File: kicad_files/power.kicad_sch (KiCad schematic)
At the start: 22 parts, among them J10 Battery Connector, U11 LT1963AxST-3.3, U14 TPS54331DR

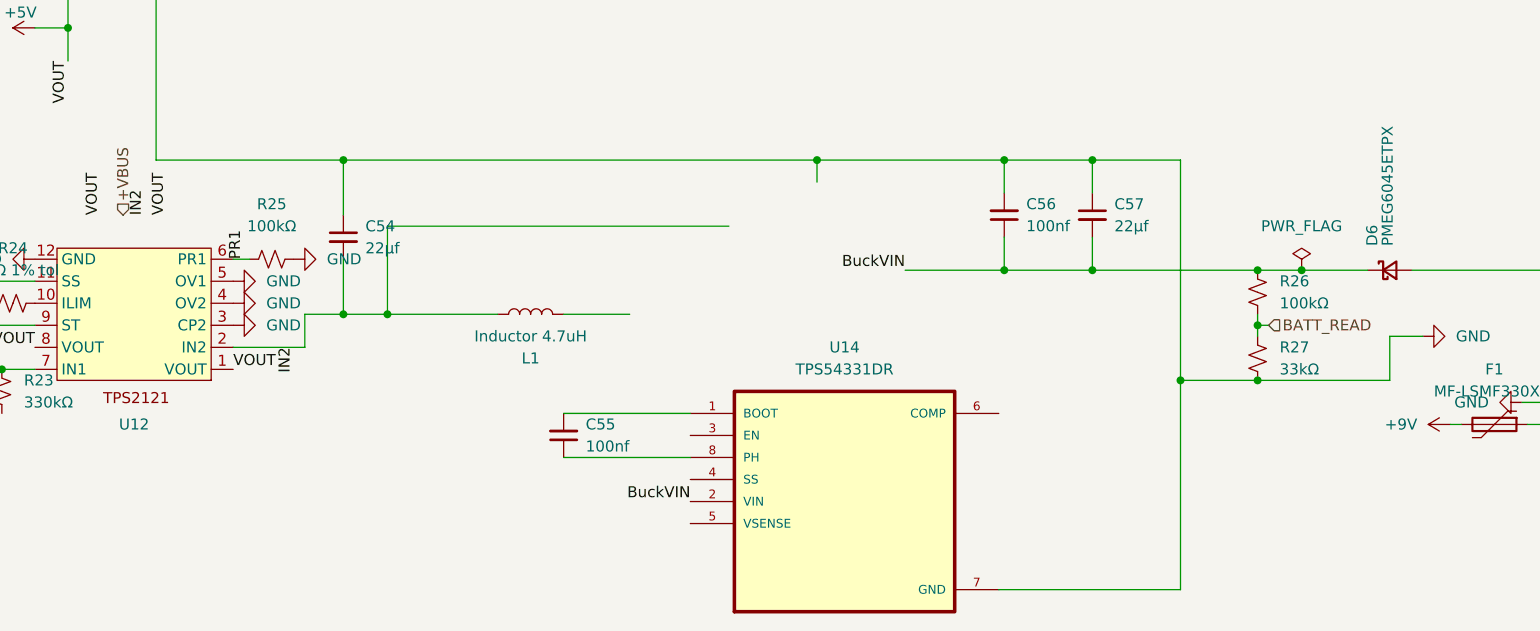
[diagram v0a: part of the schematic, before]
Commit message: fix schem for buck conv
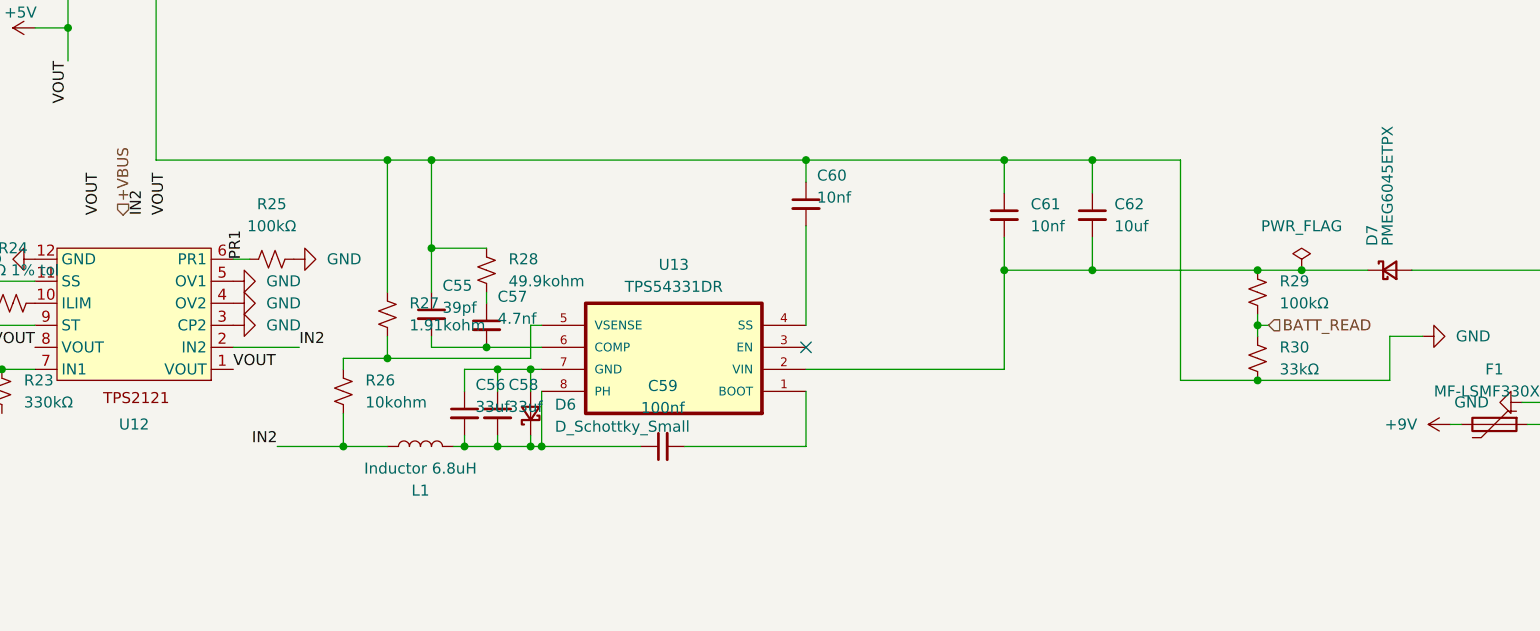
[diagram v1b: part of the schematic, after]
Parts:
- removed C54: 22μf, Capacitor_SMD:C_0805_2012Metric, symbol Device:C_Small
- added C55: 39pf, Capacitor_SMD:C_0402_1005Metric, symbol Device:C_Small
- added C58: 33uf, Capacitor_SMD:C_0805_2012Metric, symbol Device:C_Small
- added C60, C61: 10nf, Capacitor_SMD:C_0402_1005Metric, symbol Device:C_Small
- added C62: 10uf, Capacitor_SMD:C_0805_2012Metric, symbol Device:C_Small
- added D6: D_Schottky_Small, Diode_SMD:D_SMA, symbol Device:D_Schottky_Small
- added R26: 10kohm, Resistor_SMD:R_0402_1005Metric, symbol Device:R_Small_US
- added R27: 1.91kohm, Resistor_SMD:R_0402_1005Metric, symbol Device:R_Small_US
- added R28: 49.9kohm, Resistor_SMD:R_0402_1005Metric, symbol Device:R_Small_US
- C56: value 100nf -> 33uf; footprint Capacitor_SMD:C_0402_1005Metric -> Capacitor_SMD:C_0805_2012Metric
- C57: value 22μf -> 4.7nf; footprint Capacitor_SMD:C_0805_2012Metric -> Capacitor_SMD:C_0402_1005Metric
- L1: value Inductor 4.7uH -> Inductor 6.8uH
- renumbered C55 to C59, D6 to D7, R26 to R29, R27 to R30, U14 to U13
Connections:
- net GND: now also C55.1, C60.1, C61.1, C62.1, R27.1, R28.1; no longer C56.2, C57.1, U13.7 (GND)
- net IN2: now also R26.2
- net at C59.1, U13.8 (PH): now also C56.2, L1.2, C58.2, D6.1 (K)
- net at U13.4 (SS): now also C60.2
- net at U13.5 (VSENSE): now also R26.1, R27.2
- net at U13.6 (COMP): now also C57.2, C55.2
- net BuckVIN: no longer names the net of D7.1 (K), R29.1, U13.2 (VIN)
- net BuckVIN: now also C61.2, C62.2; no longer C56.1, C57.2
- new net: C56.1, C58.1, D6.2 (A), U13.7 (GND)
- new net: C57.1, R28.2
- no-connect marks 0 -> 1
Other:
- moved on the sheet: C59, L1, U13

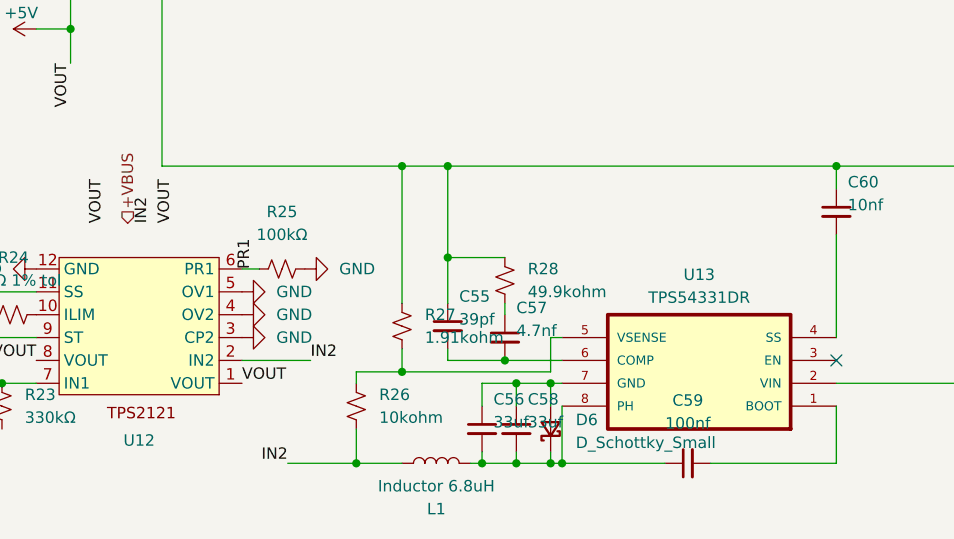
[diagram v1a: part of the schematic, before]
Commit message: replace buck converter on pcb
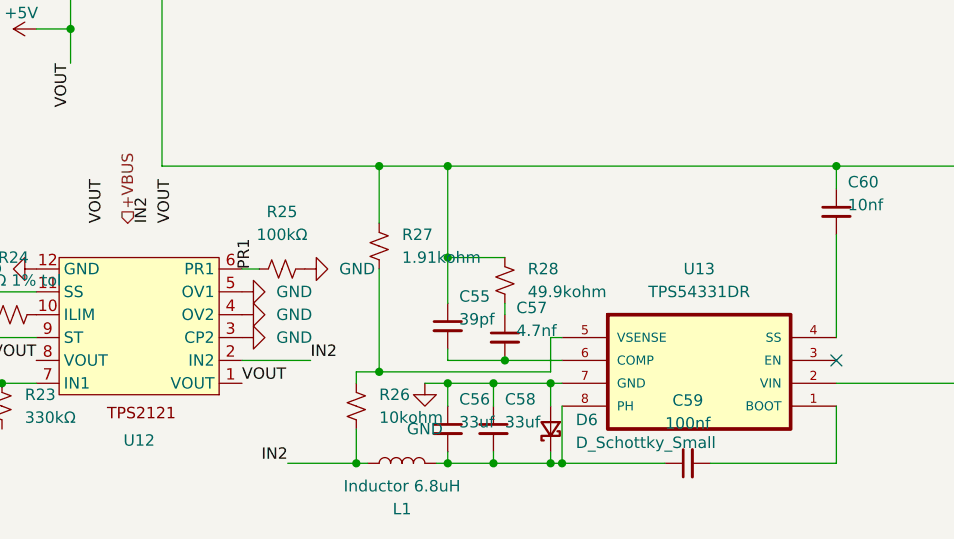
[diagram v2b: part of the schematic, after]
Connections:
- net GND: now also C56.1, C58.1, D6.2 (A), U13.7 (GND)
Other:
- moved on the sheet: C56, C58, L1, R27, U13

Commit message: fix buzzer
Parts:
- L1: footprint Inductor_SMD:L_1008_2520Metric -> Inductor_SMD:L_Coilcraft_XxL4030
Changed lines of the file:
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@@
 			)
 		)
-		(property "Footprint" "Inductor_SMD:L_1008_2520Metric"
+		(property "Footprint" "Inductor_SMD:L_Coilcraft_XxL4030"
 			(at 77.47 154.94 0)
 			(hide yes)

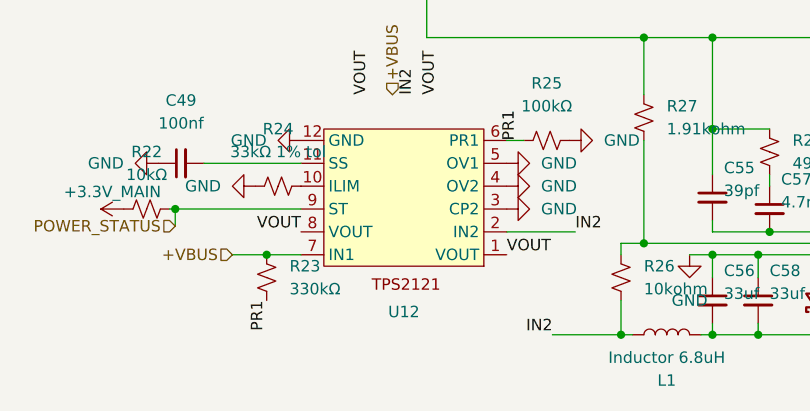
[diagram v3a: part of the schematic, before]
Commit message: fill out footprints
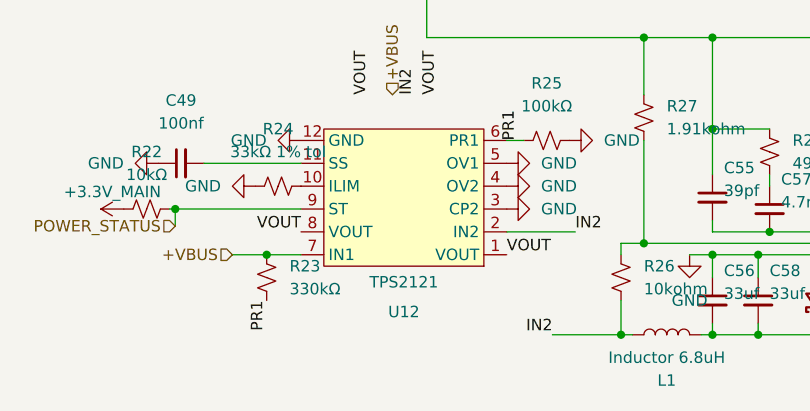
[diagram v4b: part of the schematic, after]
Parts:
- U12: value (none) -> TPS2121
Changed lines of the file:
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@@
 			)
 		)
-		(property "Value" ""
-			(at 48.26 140.97 0)
+		(property "Value" "TPS2121"
+			(at 48.26 149.098 0)
 			(show_name no)
 			(do_not_autoplace no)
@@
 		(in_pos_files yes)
 		(dnp no)
-		(fields_autoplaced yes)
 		(property "Reference" "R24"
 			(at 34.29 132.08 90)

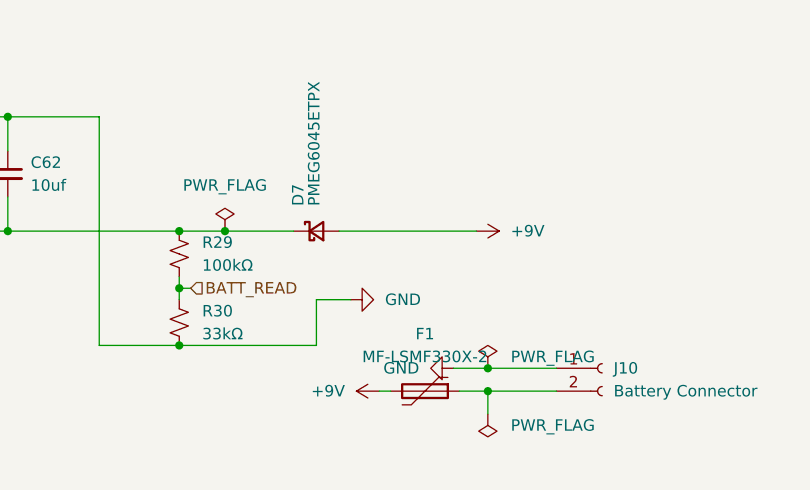
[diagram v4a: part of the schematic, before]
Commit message: JLCPCB LIBRARY IS COMPLETE
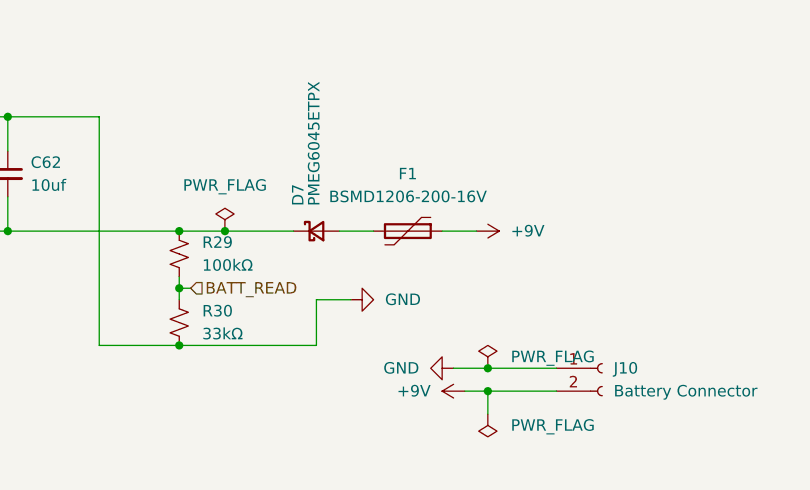
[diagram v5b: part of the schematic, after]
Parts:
- F1: value MF-LSMF330X-2 -> BSMD1206-200-16V; footprint Fuse:Fuse_Bourns_MF-SM_7.98x5.44mm -> Fuse:Fuse_1206_3216Metric
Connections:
- net +9V: now also F1.1, J10.2 (Pin_2); no longer D7.2 (A), F1.2
- new net: D7.2 (A), F1.2
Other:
- moved on the sheet: F1
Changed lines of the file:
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@@
+	(wire
+		(pts
+			(xy 209.55 152.4) (xy 212.09 152.4)
+		)
+		(stroke
+			(width 0)
+			(type default)
+		)
+	)
 	(wire
 		(pts
@@
 	(wire
 		(pts
-			(xy 195.58 134.62) (xy 210.82 134.62)
+			(xy 195.58 134.62) (xy 199.39 134.62)
 		)
 		(stroke
@@
 	(wire
 		(pts
-			(xy 200.025 152.4) (xy 201.295 152.4)
-		)
-		(stroke
-			(width 0)
-			(type default)
-		)
-	)
-	(wire
-		(pts
 			(xy 72.39 144.78) (xy 74.93 144.78)
 		)
@@
 	(wire
 		(pts
-			(xy 208.915 152.4) (xy 212.09 152.4)
-		)
-		(stroke
-			(width 0)
-			(type default)
-		)
-	)
-	(wire
-		(pts
 			(xy 82.55 146.05) (xy 87.63 146.05)
 		)
@@
 		(pts
 			(xy 95.25 146.05) (xy 93.98 146.05)
+		)
+		(stroke
+			(width 0)
+			(type default)
+		)
+	)
+	(wire
+		(pts
+			(xy 207.01 134.62) (xy 210.82 134.62)
 		)
 		(stroke
@@
 	(symbol
 		(lib_id "power:+9V")
-		(at 200.025 152.4 90)
+		(at 209.55 152.4 90)
 		(unit 1)
 		(body_style 1)
@@
 		(fields_autoplaced yes)
 		(property "Reference" "#PWR090"
-			(at 203.835 152.4 0)
+			(at 213.36 152.4 0)
 			(hide yes)
 			(show_name no)
@@
 		)
 		(property "Value" "+9V"
-			(at 196.215 152.3999 90)
+			(at 205.74 152.3999 90)
 			(show_name no)
 			(do_not_autoplace no)
@@
 		)
 		(property "Footprint" ""
-			(at 200.025 152.4 0)
+			(at 209.55 152.4 0)
 			(hide yes)
 			(show_name no)
@@
 		)
 		(property "Datasheet" ""
-			(at 200.025 152.4 0)
+			(at 209.55 152.4 0)
 			(hide yes)
 			(show_name no)
@@
 		)
 		(property "Description" "Power symbol creates a global label with name \"+9V\""
-			(at 200.025 152.4 0)
+			(at 209.55 152.4 0)
 			(hide yes)
 			(show_name no)
@@
 	(symbol
 		(lib_id "Device:Polyfuse")
-		(at 205.105 152.4 270)
+		(at 203.2 134.62 270)
 		(unit 1)
 		(body_style 1)
@@
 		(fields_autoplaced yes)
 		(property "Reference" "F1"
-			(at 205.105 146.05 90)
-			(show_name no)
-			(do_not_autoplace no)
-			(effects
-				(font
-					(size 1.27 1.27)
-				)
-			)
-		)
-		(property "Value" "MF-LSMF330X-2"
-			(at 205.105 148.59 90)
-			(show_name no)
-			(do_not_autoplace no)
-			(effects
-				(font
-					(size 1.27 1.27)
-				)
-			)
-		)
-		(property "Footprint" "Fuse:Fuse_Bourns_MF-SM_7.98x5.44mm"
-			(at 200.025 153.67 0)
+			(at 203.2 128.27 90)
+			(show_name no)
+			(do_not_autoplace no)
+			(effects
+				(font
+					(size 1.27 1.27)
+				)
+			)
+		)
+		(property "Value" "BSMD1206-200-16V"
+			(at 203.2 130.81 90)
+			(show_name no)
+			(do_not_autoplace no)
+			(effects
+				(font
+					(size 1.27 1.27)
+				)
+			)
+		)
+		(property "Footprint" "Fuse:Fuse_1206_3216Metric"
+			(at 198.12 135.89 0)
 			(hide yes)
 			(show_name no)
@@
 		)
 		(property "Datasheet" ""
-			(at 205.105 152.4 0)
+			(at 203.2 134.62 0)
 			(hide yes)
 			(show_name no)
@@
 		)
 		(property "Description" "Resettable fuse, polymeric positive temperature coefficient"
-			(at 205.105 152.4 0)
-			(hide yes)
-			(show_name no)
+			(at 203.2 134.62 0)
+			(hide yes)
+			(show_name no)

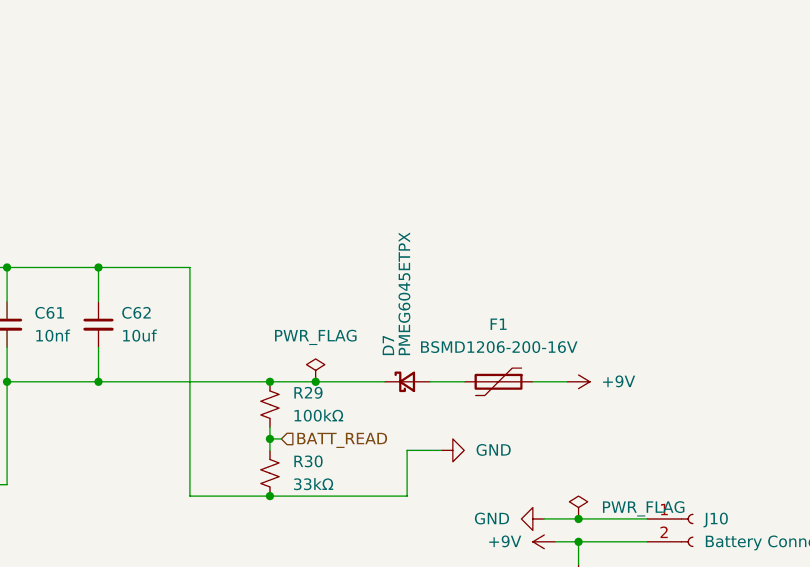
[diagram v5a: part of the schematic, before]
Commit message: change diode
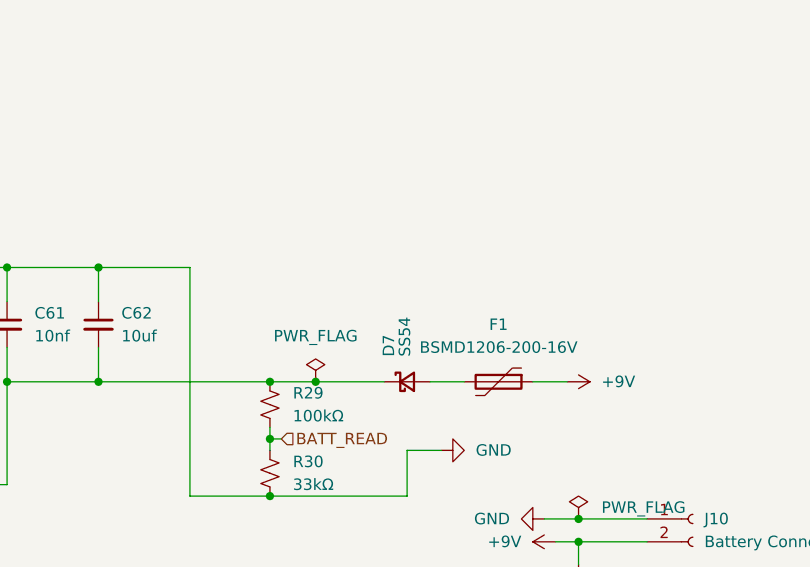
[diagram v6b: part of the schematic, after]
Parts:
- D7: value PMEG6045ETPX -> SS54; footprint Diode_SMD:D_SOD-128 -> Diode_SMD:D_SMA
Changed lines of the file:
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@@
 			)
 		)
-		(property "Value" "PMEG6045ETPX"
+		(property "Value" "SS54"
 			(at 192.786 131.826 90)
 			(show_name no)
@@
 			)
 		)
-		(property "Footprint" "Diode_SMD:D_SOD-128"
+		(property "Footprint" "Diode_SMD:D_SMA"
 			(at 193.04 134.62 90)
 			(hide yes)
